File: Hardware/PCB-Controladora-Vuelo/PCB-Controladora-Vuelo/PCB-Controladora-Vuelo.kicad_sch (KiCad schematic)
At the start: 14 parts, among them J1 Jumper Serial, J2 ESC, U1 MPU-5060, U2 ESP32-DEVKIT-V1, U2 Nrf24l01, U3 AMS1117-3.3

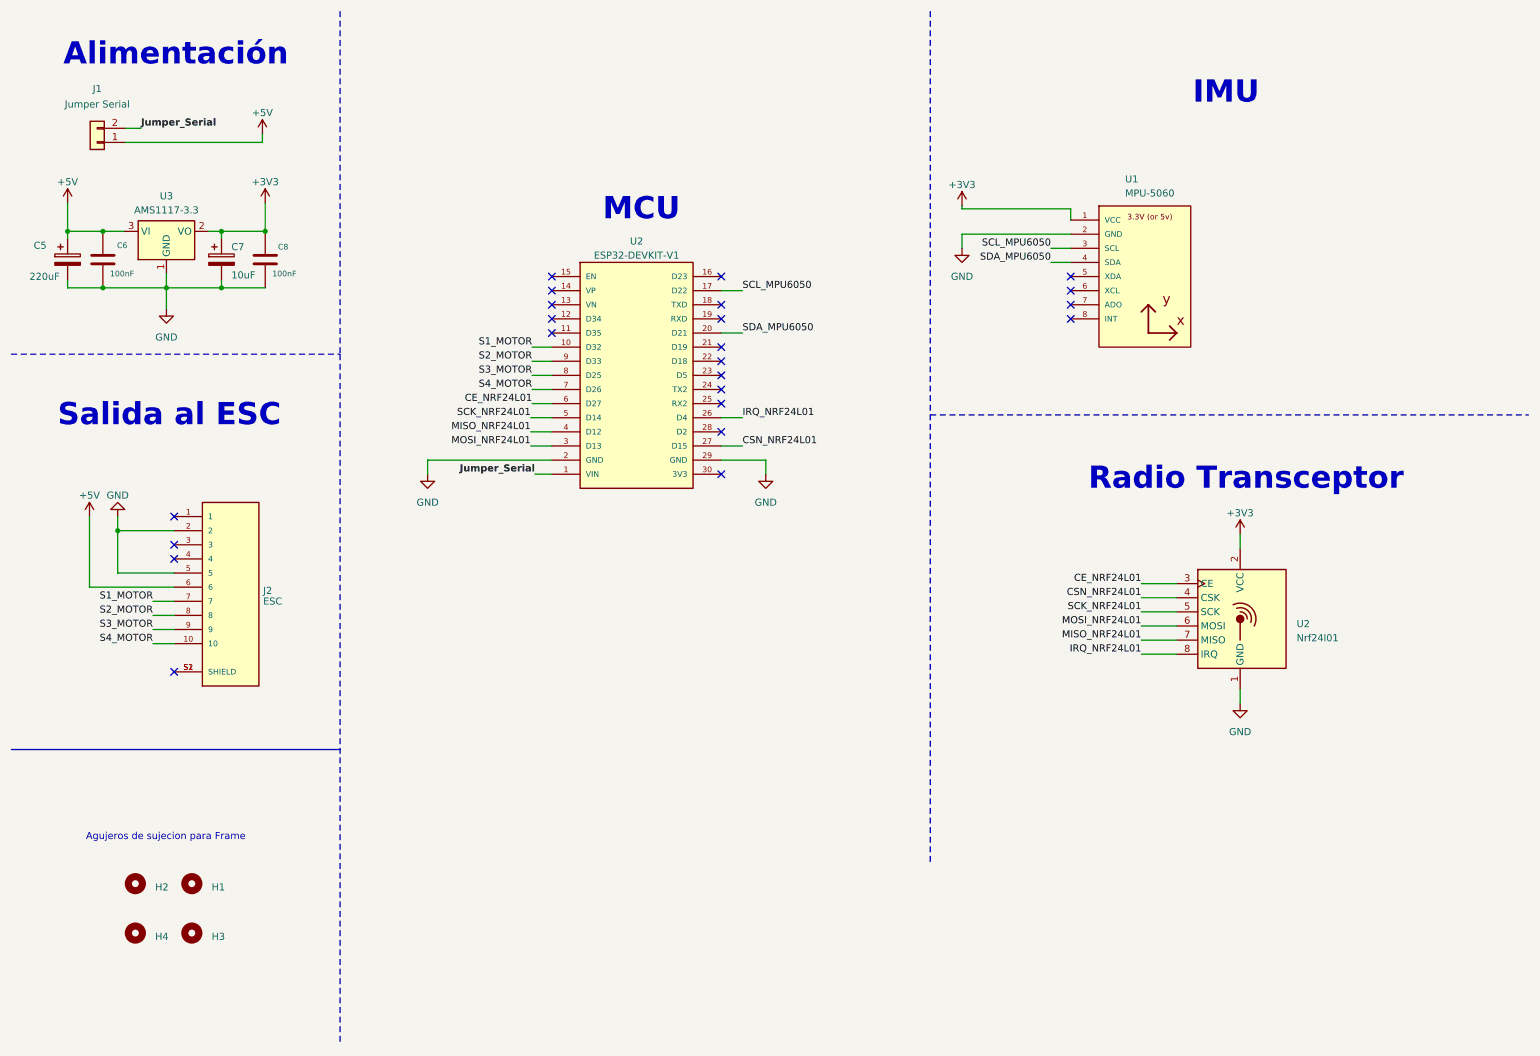
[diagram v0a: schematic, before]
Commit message: Agrego cambios en el esquematico de la nueva version de la controaldora de vuelo 2.0
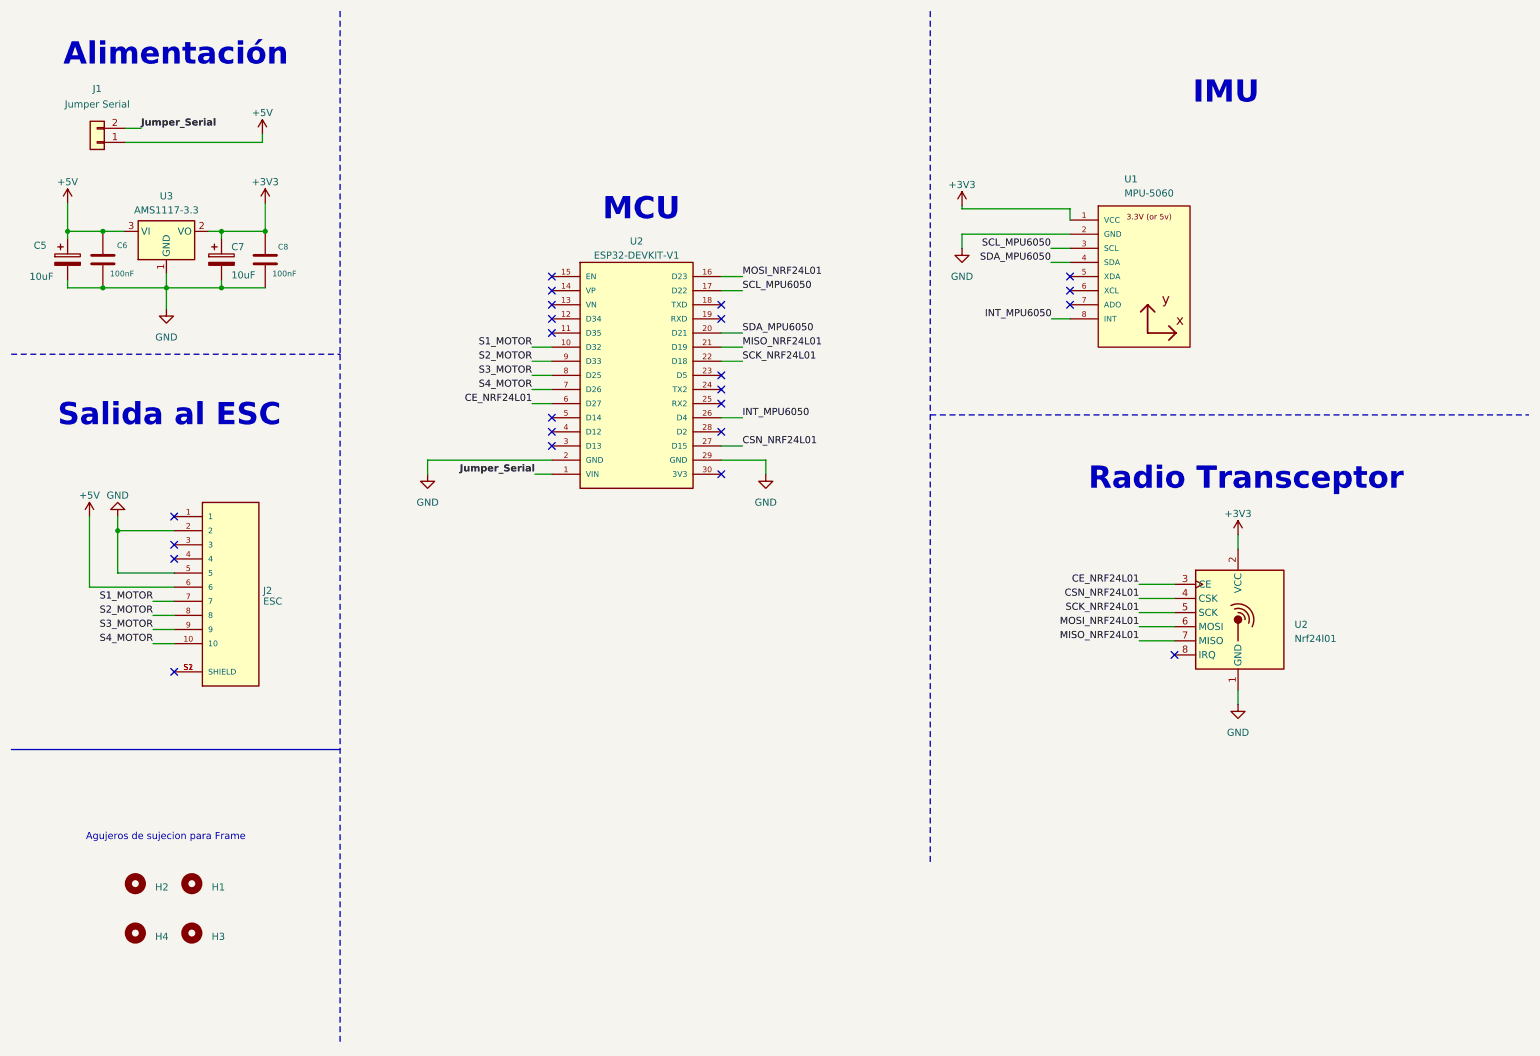
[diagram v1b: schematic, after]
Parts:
- C5: value 220uF -> 10uF; footprint Capacitor_THT:CP_Radial_D4.0mm_P1.50mm -> Capacitor_Tantalum_SMD:CP_EIA-2012-12_Kemet-R
- C7: footprint Capacitor_THT:CP_Radial_D4.0mm_P1.50mm -> Capacitor_Tantalum_SMD:CP_EIA-2012-12_Kemet-R_Pad1.30x1.05mm_HandSolder
- J1: footprint Connector_PinHeader_1.27mm:PinHeader_1x02_P1.27mm_Vertical -> Connector_PinHeader_2.54mm:PinHeader_1x02_P2.54mm_Vertical
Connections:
- net MISO_NRF24L01: now also U2.21 (D19); no longer U2.4 (D12)
- net MOSI_NRF24L01: now also U2.16 (D23); no longer U2.3 (D13)
- net SCK_NRF24L01: now also U2.22 (D18); no longer U2.5 (D14)
- net INT_MPU6050: now reaches U1.8 (INT)
- net INT_MPU6050: now also U2.26 (D4)
- net IRQ_NRF24L01: no longer names the net of U2.8 (IRQ)
- net IRQ_NRF24L01: no longer U2.26 (D4)

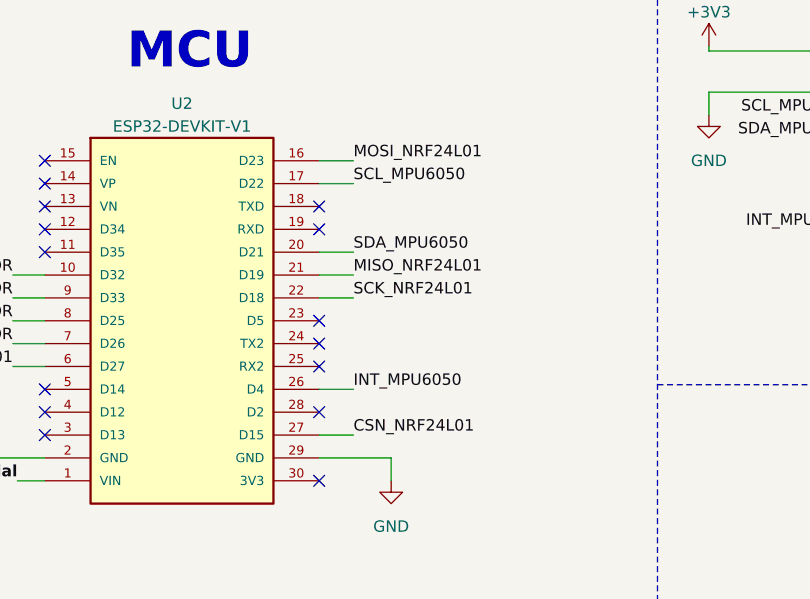
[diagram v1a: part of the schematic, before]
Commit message: Cambie pines i2c mpu6050 , hay que probarlos y cambie conexiones de nrf que funcionan, mejore las medidas para el frame
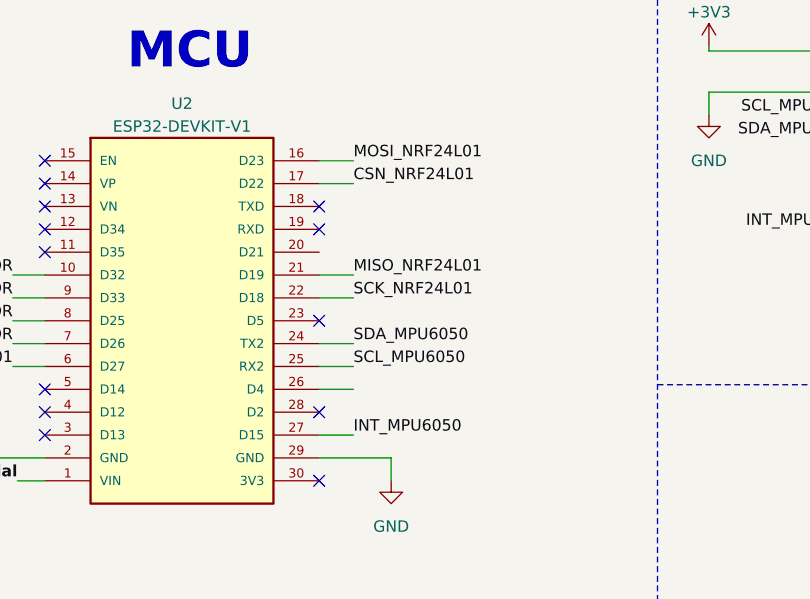
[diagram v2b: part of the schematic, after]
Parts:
- C5: footprint Capacitor_Tantalum_SMD:CP_EIA-2012-12_Kemet-R -> Capacitor_SMD:C_1206_3216Metric_Pad1.33x1.80mm_HandSolder
- C7: footprint Capacitor_Tantalum_SMD:CP_EIA-2012-12_Kemet-R_Pad1.30x1.05mm_HandSolder -> Capacitor_SMD:C_1206_3216Metric_Pad1.33x1.80mm_HandSolder
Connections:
- net CSN_NRF24L01: now also U2.17 (D22); no longer U2.27 (D15)
- net INT_MPU6050: now also U2.27 (D15); no longer U2.26 (D4)
- net SCL_MPU6050: now also U2.25 (RX2); no longer U2.17 (D22)
- net SDA_MPU6050: now also U2.24 (TX2); no longer U2.20 (D21)
- no-connect marks 23 -> 21
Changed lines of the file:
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@@
   (no_connect (at 41.275 107.95))
   (no_connect (at 41.275 130.81))
-  (no_connect (at 139.7 80.01))
-  (no_connect (at 139.7 82.55))
   (wire (pts (xy 147.701 95.25) (xy 147.701 92.71))
     (stroke (width 0) (type default))
@@
     (stroke (width 0) (type default))
   )
-  (wire (pts (xy 143.51 69.85) (xy 139.7 69.85))
-    (stroke (width 0) (type default))
-  )
   (wire (pts (xy 22.098 46.482) (xy 22.098 51.562))
     (stroke (width 0) (type default))
@@
     (stroke (width 0) (type default))
   )
+  (wire (pts (xy 139.7 80.01) (xy 143.51 80.01))
+    (stroke (width 0) (type default))
+  )
   (wire (pts (xy 28.448 61.722) (xy 39.878 61.722))
     (stroke (width 0) (type default))
@@
     (stroke (width 0) (type default))
   )
+  (wire (pts (xy 139.7 82.55) (xy 143.51 82.55))
+    (stroke (width 0) (type default))
+  )
   (wire (pts (xy 49.784 51.562) (xy 49.784 52.832))
     (stroke (width 0) (type default))
@@
     (effects (font (size 4 4) (thickness 0.8) bold) (justify left bottom))
   )
-  (label "INT_MPU6050" (at 143.51 85.09 0) (fields_autoplaced)
-    (effects (font (size 1.27 1.27)) (justify left bottom))
-  )
   (label "SDA_MPU6050" (at 199.009 57.15 180) (fields_autoplaced)
     (effects (font (size 1.27 1.27)) (justify right bottom))
@@
     (effects (font (size 1.27 1.27)) (justify right bottom))
   )
-  (label "SDA_MPU6050" (at 143.51 69.85 0) (fields_autoplaced)
-    (effects (font (size 1.27 1.27)) (justify left bottom))
-  )
   (label "SCL_MPU6050" (at 199.009 54.61 180) (fields_autoplaced)
     (effects (font (size 1.27 1.27)) (justify right bottom))
   )
-  (label "CSN_NRF24L01" (at 143.51 90.17 0) (fields_autoplaced)
-    (effects (font (size 1.27 1.27)) (justify left bottom))
-  )
   (label "S3_MOTOR" (at 105.664 77.47 180) (fields_autoplaced)
     (effects (font (size 1.27 1.27)) (justify right bottom))
@@
     (effects (font (size 1.27 1.27) bold) (justify left bottom))
   )
+  (label "INT_MPU6050" (at 143.51 90.17 0) (fields_autoplaced)
+    (effects (font (size 1.27 1.27)) (justify left bottom))
+  )
   (label "INT_MPU6050" (at 199.136 67.31 180) (fields_autoplaced)
     (effects (font (size 1.27 1.27)) (justify right bottom))
   )
+  (label "SCL_MPU6050" (at 143.51 82.55 0) (fields_autoplaced)
+    (effects (font (size 1.27 1.27)) (justify left bottom))
+  )
   (label "S4_MOTOR" (at 37.465 125.73 180) (fields_autoplaced)
     (effects (font (size 1.27 1.27)) (justify right bottom))
@@
     (effects (font (size 1.27 1.27)) (justify right bottom))
   )
-  (label "SCL_MPU6050" (at 143.51 62.23 0) (fields_autoplaced)
+  (label "SDA_MPU6050" (at 143.51 80.01 0) (fields_autoplaced)
     (effects (font (size 1.27 1.27)) (justify left bottom))
   )
@@
     (effects (font (size 1.27 1.27)) (justify right bottom))
   )
+  (label "CSN_NRF24L01" (at 143.51 62.23 0) (fields_autoplaced)
+    (effects (font (size 1.27 1.27)) (justify left bottom))
+  )
   (label "S1_MOTOR" (at 37.465 118.11 180) (fields_autoplaced)
     (effects (font (size 1.27 1.27)) (justify right bottom))
@@
       (effects (font (size 1.27 1.27)) (justify left))
     )
-    (property "Footprint" "Capacitor_Tantalum_SMD:CP_EIA-2012-12_Kemet-R_Pad1.30x1.05mm_HandSolder" (at 50.7492 60.452 0)
+    (property "Footprint" "Capacitor_SMD:C_1206_3216Metric_Pad1.33x1.80mm_HandSolder" (at 50.7492 60.452 0)
       (effects (font (size 1.27 1.27)) hide)
     )
@@
       (effects (font (size 1.27 1.27)) (justify left))
     )
-    (property "Footprint" "Capacitor_Tantalum_SMD:CP_EIA-2012-12_Kemet-R" (at 23.0632 60.452 0)
+    (property "Footprint" "Capacitor_SMD:C_1206_3216Metric_Pad1.33x1.80mm_HandSolder" (at 23.0632 60.452 0)
       (effects (font (size 1.27 1.27)) hide)
     )

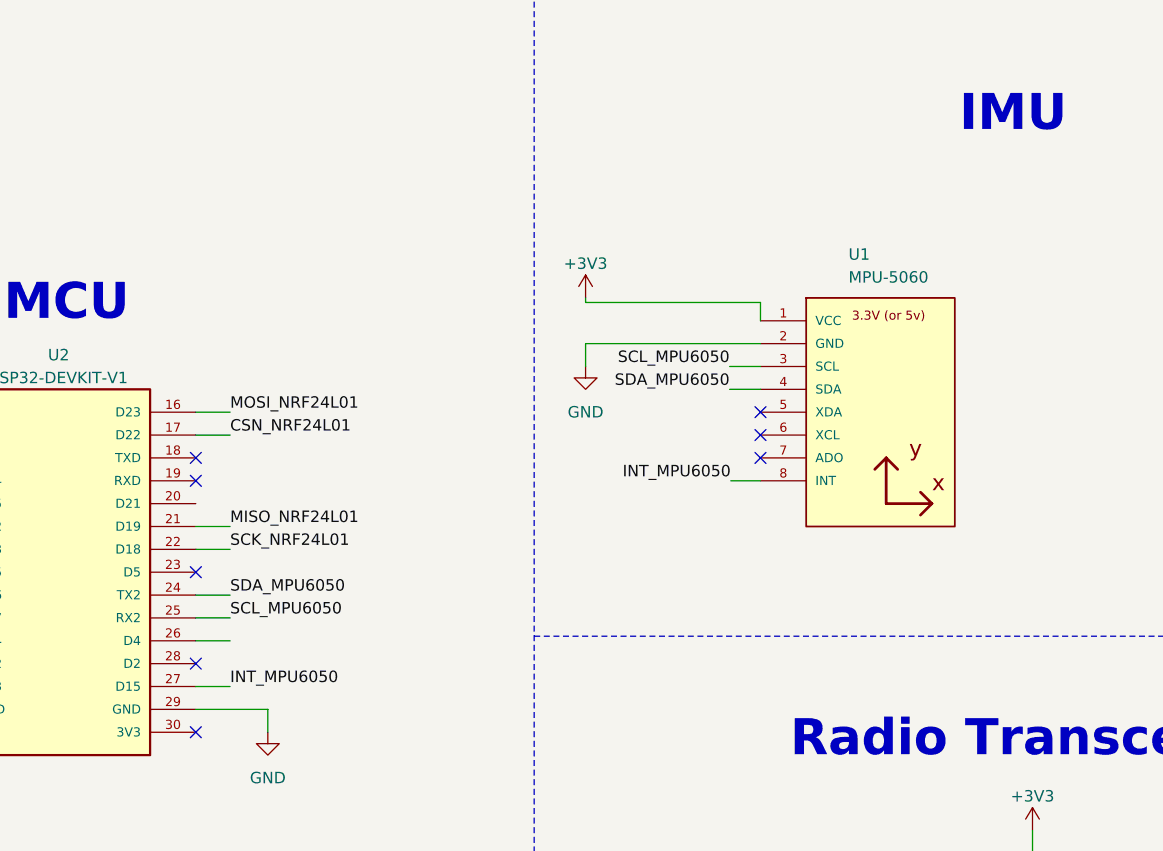
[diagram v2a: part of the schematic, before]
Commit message: cambie pines sda y scl para evitar conflictos wifi
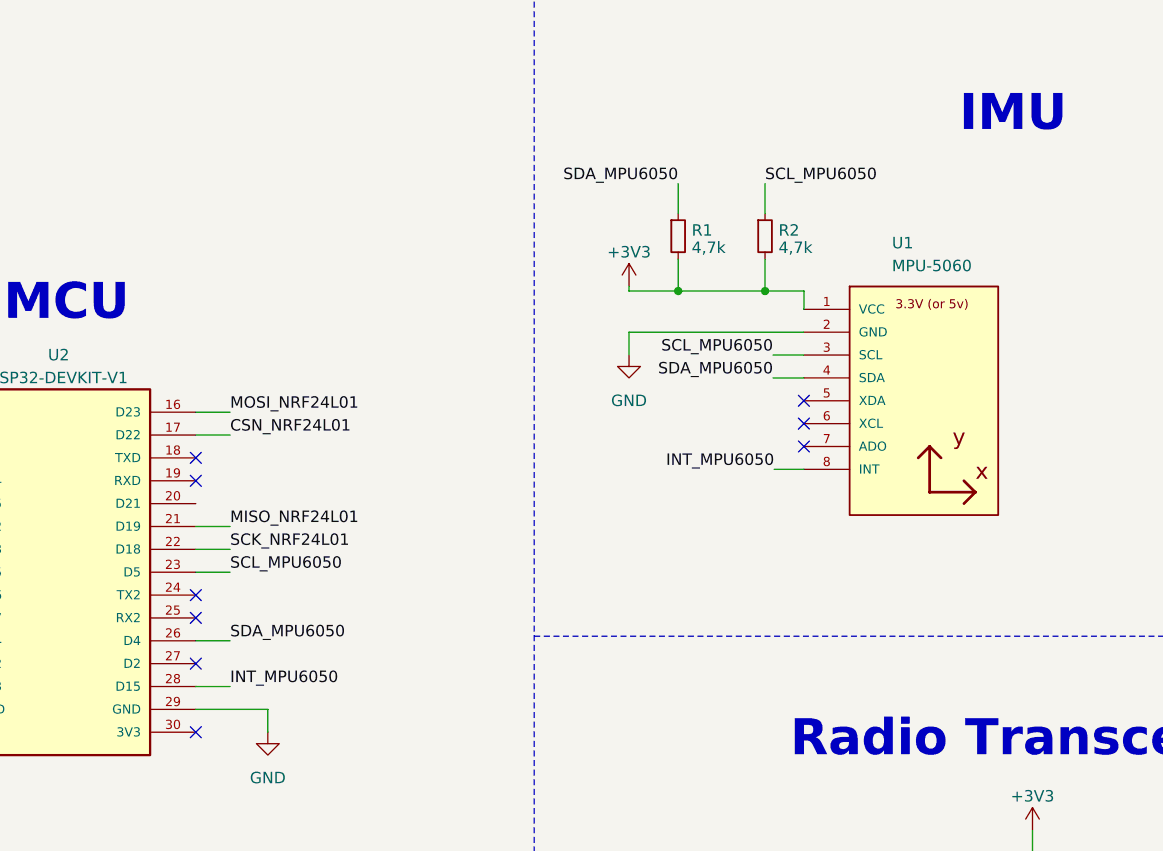
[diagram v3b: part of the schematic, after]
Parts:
- added R1, R2: 4,7k, Resistor_SMD:R_1206_3216Metric_Pad1.30x1.75mm_HandSolder, symbol Device:R_Small
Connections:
- net +3V3: now also R1.2, R2.2
- net INT_MPU6050: now also U2.28 (D15); no longer U2.27 (D15)
- net SCL_MPU6050: now also U2.23 (D5), R2.1; no longer U2.25 (RX2)
- net SDA_MPU6050: now also U2.26 (D4), R1.1; no longer U2.24 (TX2)
- no-connect marks 21 -> 22
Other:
- moved on the sheet: U1
